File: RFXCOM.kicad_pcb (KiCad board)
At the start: 2 copper layers, 23 x 45.8 mm, 9 parts, among them J1 Conn_Coaxial, J2 Conn_Coaxial, J3 Conn_01x01, J4 Rx, J5 Tx, U1 arduino_mega_pro_embedded

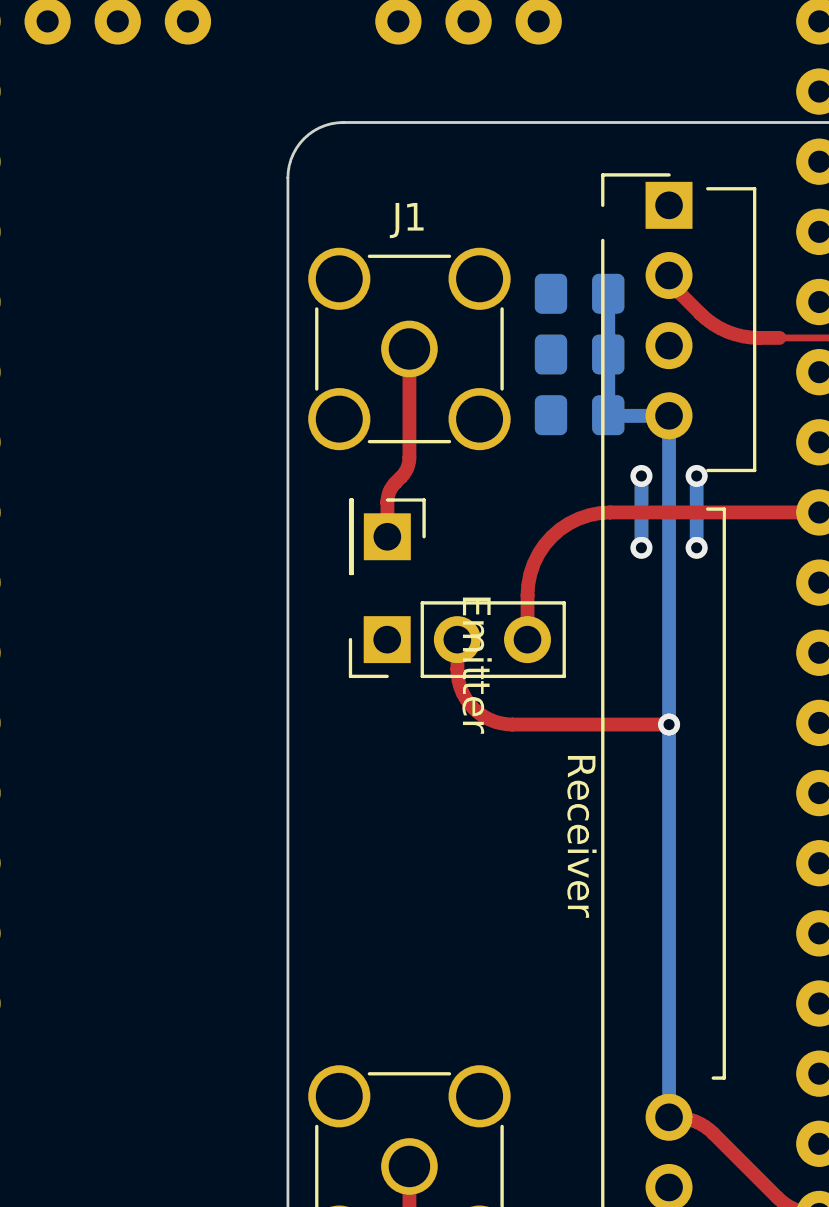
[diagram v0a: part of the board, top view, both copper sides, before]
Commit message: Fix labels on pcb, add screenshot
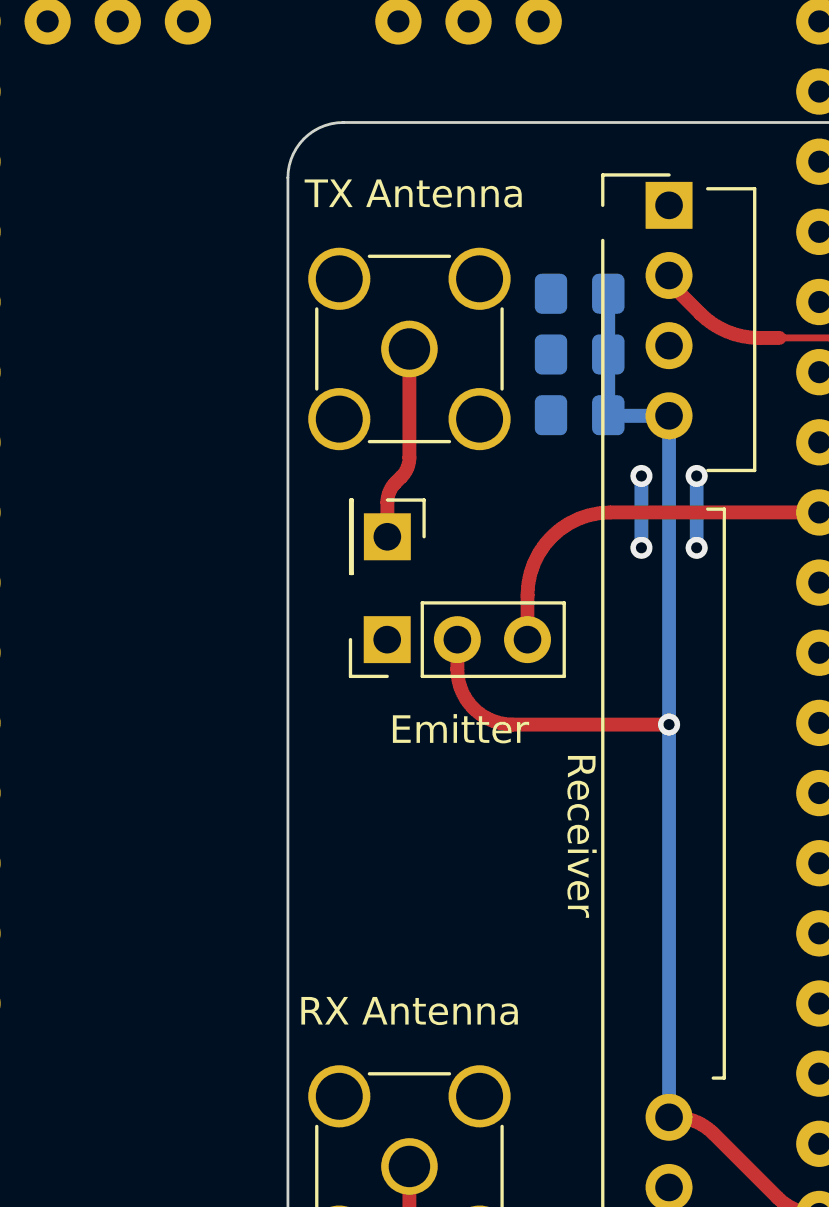
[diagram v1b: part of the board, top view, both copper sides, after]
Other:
- board text added: "100n 470n 10µ"
- board text added: "RX Antenna"
- board text added: "TX Antenna"
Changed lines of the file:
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@@
     (property "Sheetname" "")
     (attr through_hole)
-    (fp_text reference "J1" (at 0 -4.75) (layer "F.SilkS")
+    (fp_text reference "J1" (at 0 -4.75) (layer "F.SilkS") hide
       (effects (font (size 1 1) (thickness 0.15)))
     )
@@
     (property "Sheetname" "")
     (attr smd)
-    (fp_text reference "C2" (at 2.6 0 90) (layer "B.SilkS")
+    (fp_text reference "C2" (at 2.6 0 90) (layer "B.SilkS") hide
       (effects (font (size 1 1) (thickness 0.15)) (justify mirror))
     )
@@
     (property "Sheetname" "")
     (attr smd)
-    (fp_text reference "C3" (at 2.6 0 90) (layer "B.SilkS")
+    (fp_text reference "C3" (at 0.9625 -2 90) (layer "B.SilkS") hide
       (effects (font (size 1 1) (thickness 0.15)) (justify mirror))
     )
@@
     (property "Sheetname" "")
     (attr smd)
-    (fp_text reference "C1" (at 2.6 0 90) (layer "B.SilkS")
+    (fp_text reference "C1" (at 0.9625 2 90) (layer "B.SilkS") hide
       (effects (font (size 1 1) (thickness 0.15)) (justify mirror))
     )
@@
   (gr_arc (start 112 91.4) (mid 110.585786 90.814214) (end 110 89.4) (layer "Edge.Cuts") (width 0.1))
   (gr_line (start 133 91.4) (end 112 91.4) (layer "Edge.Cuts") (width 0.1))
+  (gr_text "100n\n470n\n 10µ" (at 120.4 59.6) (layer "B.SilkS")
+    (effects (font (size 1 1) (thickness 0.15)) (justify mirror))
+  )
   (gr_text "Receiver" (at 120.6 71.4 -90) (layer "F.SilkS")
     (effects (font (size 1 1) (thickness 0.15)))
   )
-  (gr_text "Emitter" (at 116.8 65.2 270) (layer "F.SilkS")
-    (effects (font (size 1 1) (thickness 0.15)))
-  )
+  (gr_text "RX Antenna" (at 114.4 77.8) (layer "F.SilkS")
+    (effects (font (size 1 1) (thickness 0.15)))
+  )
+  (gr_text "TX Antenna" (at 114.6 48.2) (layer "F.SilkS")
+    (effects (font (size 1 1) (thickness 0.15)))
+  )
+  (gr_text "Emitter" (at 116.2 67.6) (layer "F.SilkS")
+    (effects (font (size 1 1) (thickness 0.15)))
+  )

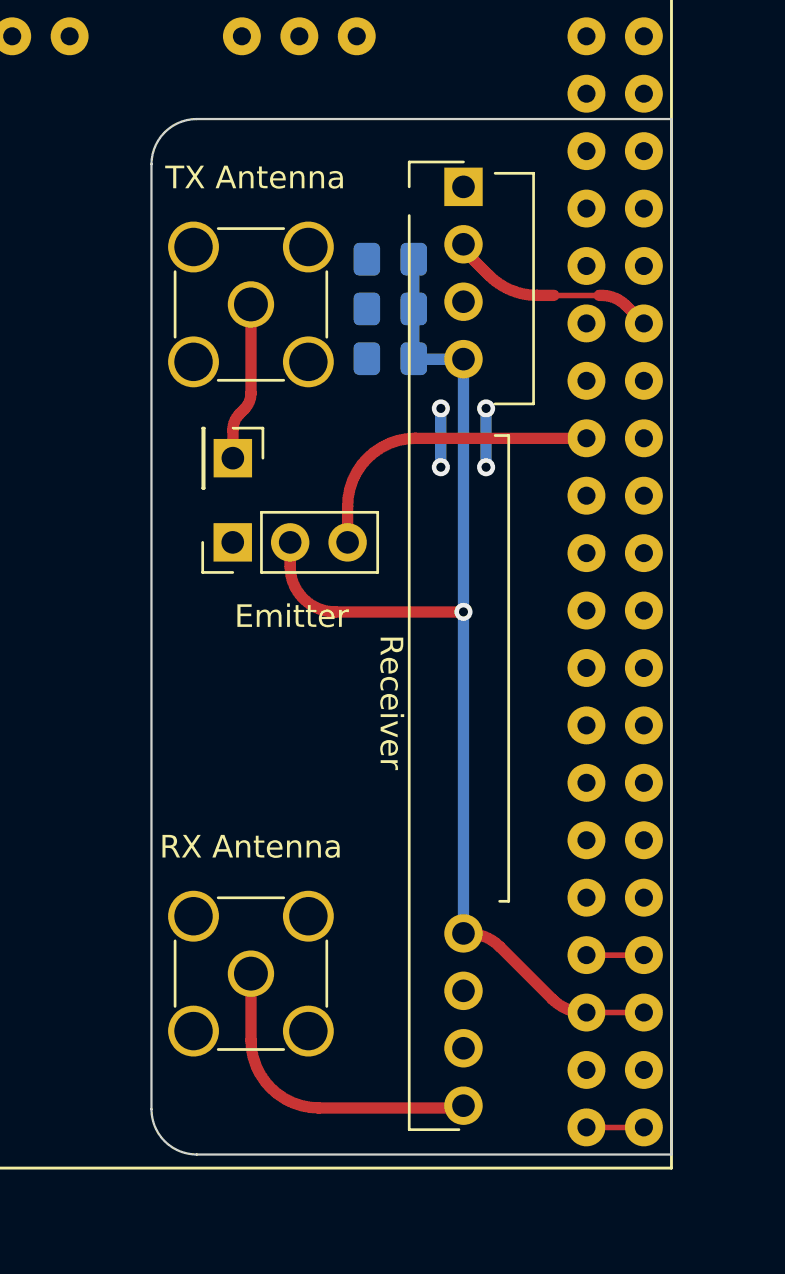
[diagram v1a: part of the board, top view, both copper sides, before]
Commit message: Use correct footprint for TX
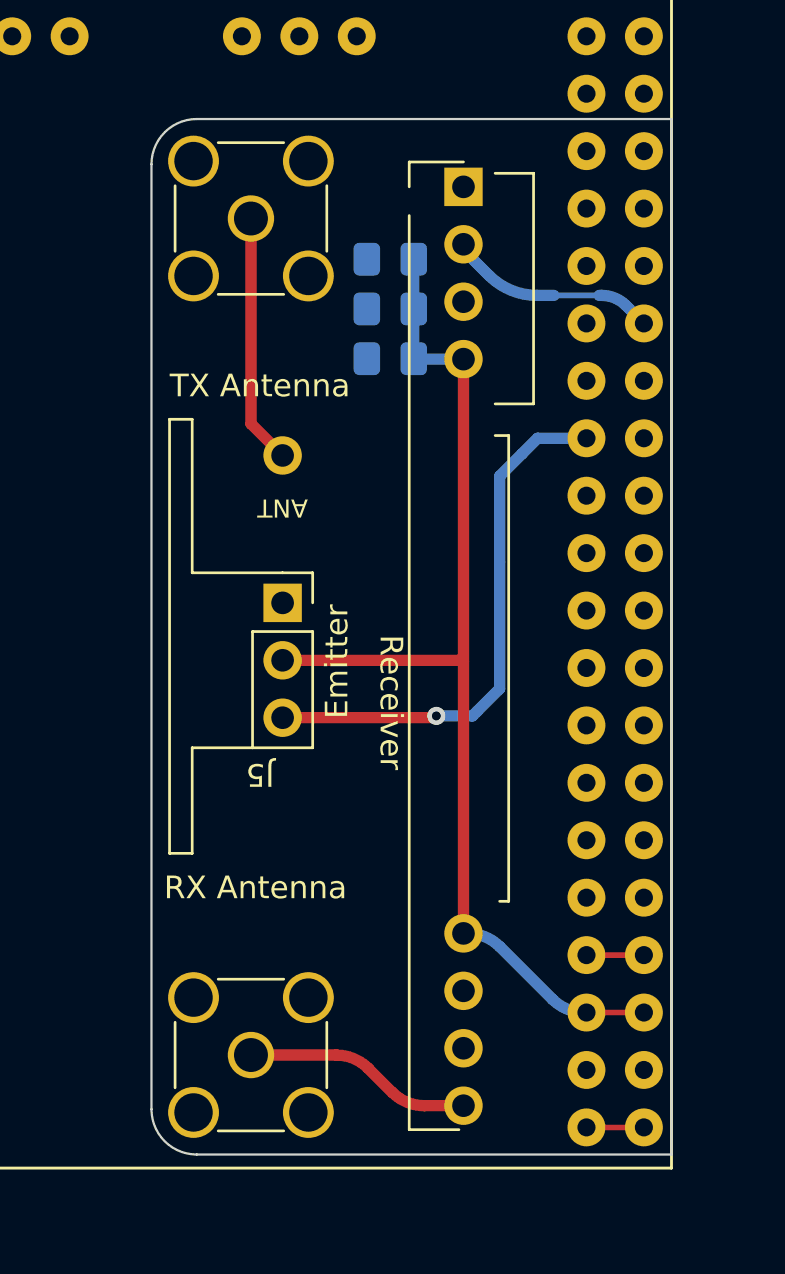
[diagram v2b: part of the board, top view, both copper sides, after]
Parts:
- removed J3: Conn_01x01, Connector_PinHeader_2.54mm:PinHeader_1x01_P2.54mm_Vertical
- J5: footprint Connector_PinHeader_2.54mm:PinHeader_1x03_P2.54mm_Vertical -> rf_components:XKFST_Vertical
- moved J1 3.80 mm to (114.4, 50.0)
- moved J2 3.60 mm to (114.4, 87.0)
- moved J5 3.47 mm to (115.8, 67.0), turned to 180 degrees
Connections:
- J1 pad 1: Net-(J3-Pad1) -> Net-(J5-Pad4)
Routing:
- net Net-(J5-Pad4): track 0.00 -> 11.1 mm
- net /Tx_DATA: track 13.9 -> 24.1 mm, vias 0 -> 1
- net Net-(J3-Pad1): track 7.04 -> 0.00 mm
- net GND: track 5.20 -> 0.00 mm, vias 4 -> 0
- net /antenne: track 14.0 -> 10.3 mm
- net +5V: track 51.1 -> 49.3 mm, vias 1 -> 0
